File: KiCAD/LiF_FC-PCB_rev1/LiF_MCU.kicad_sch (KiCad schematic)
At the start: 13 parts, among them J4 USB_C_Receptacle_USB2.0_14P, Q3 MMBT4401, Q4 MMBT4401, U4 ESP32-S3-WROOM-1, U5 MCP2200T-E-SS, Y2 12MHz

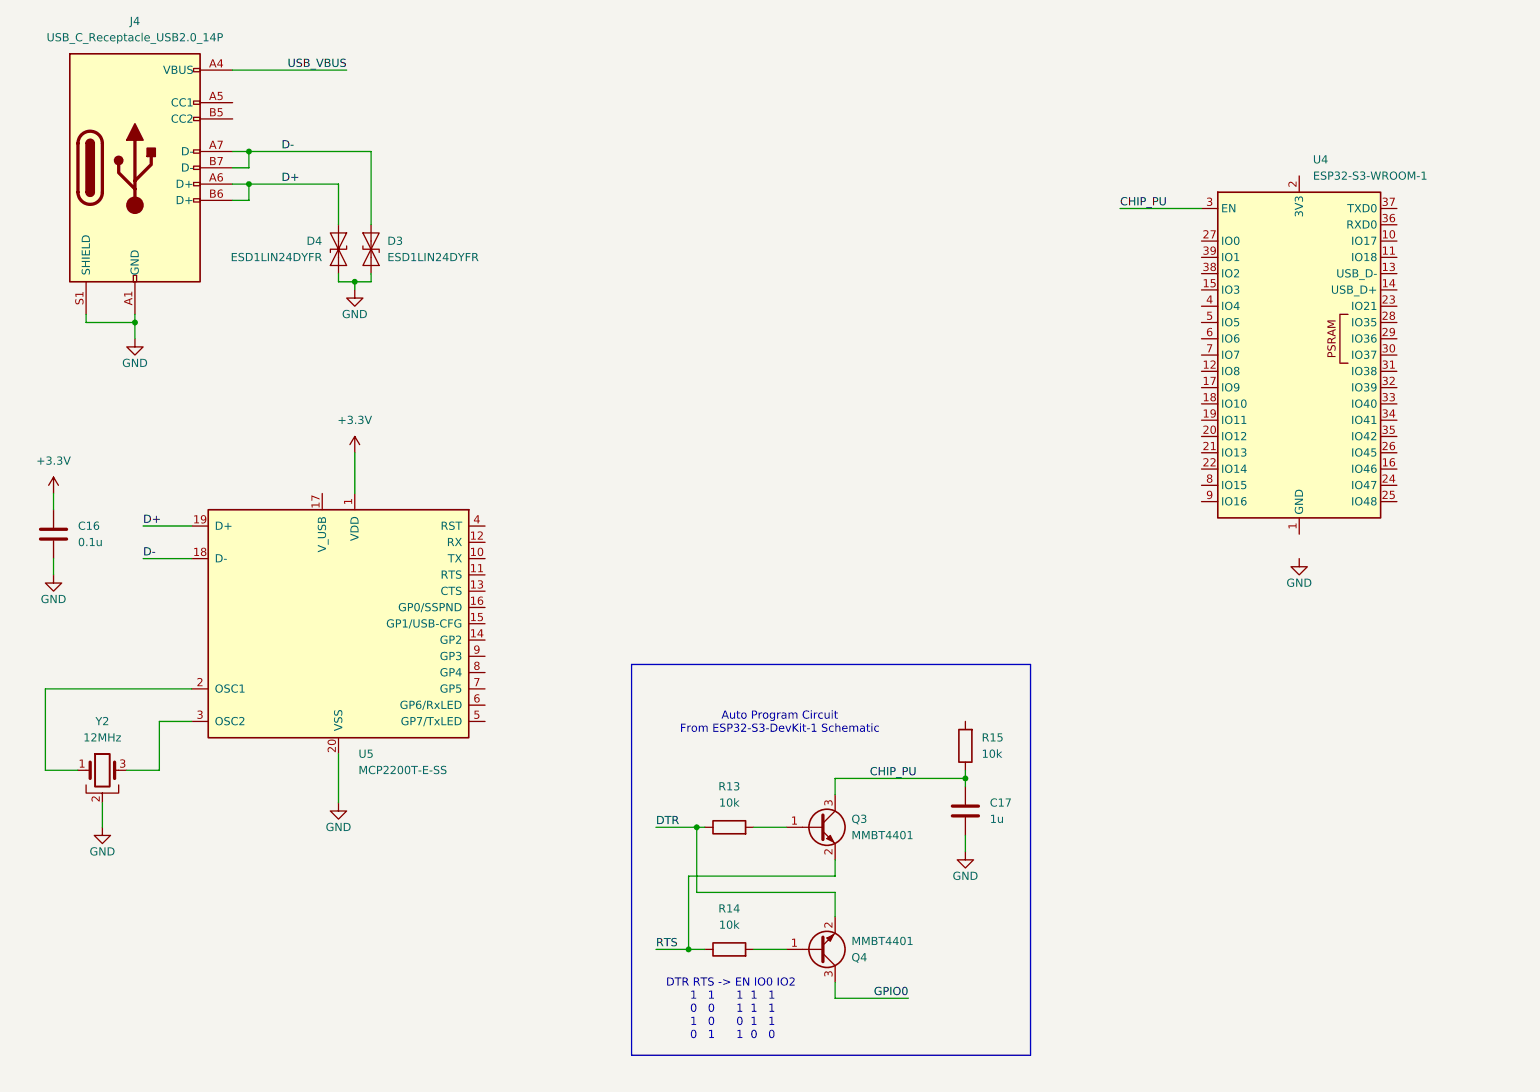
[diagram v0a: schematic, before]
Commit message: replaced a USB to UART bridge to support auto-programming of ESP, added reset and flash buttons
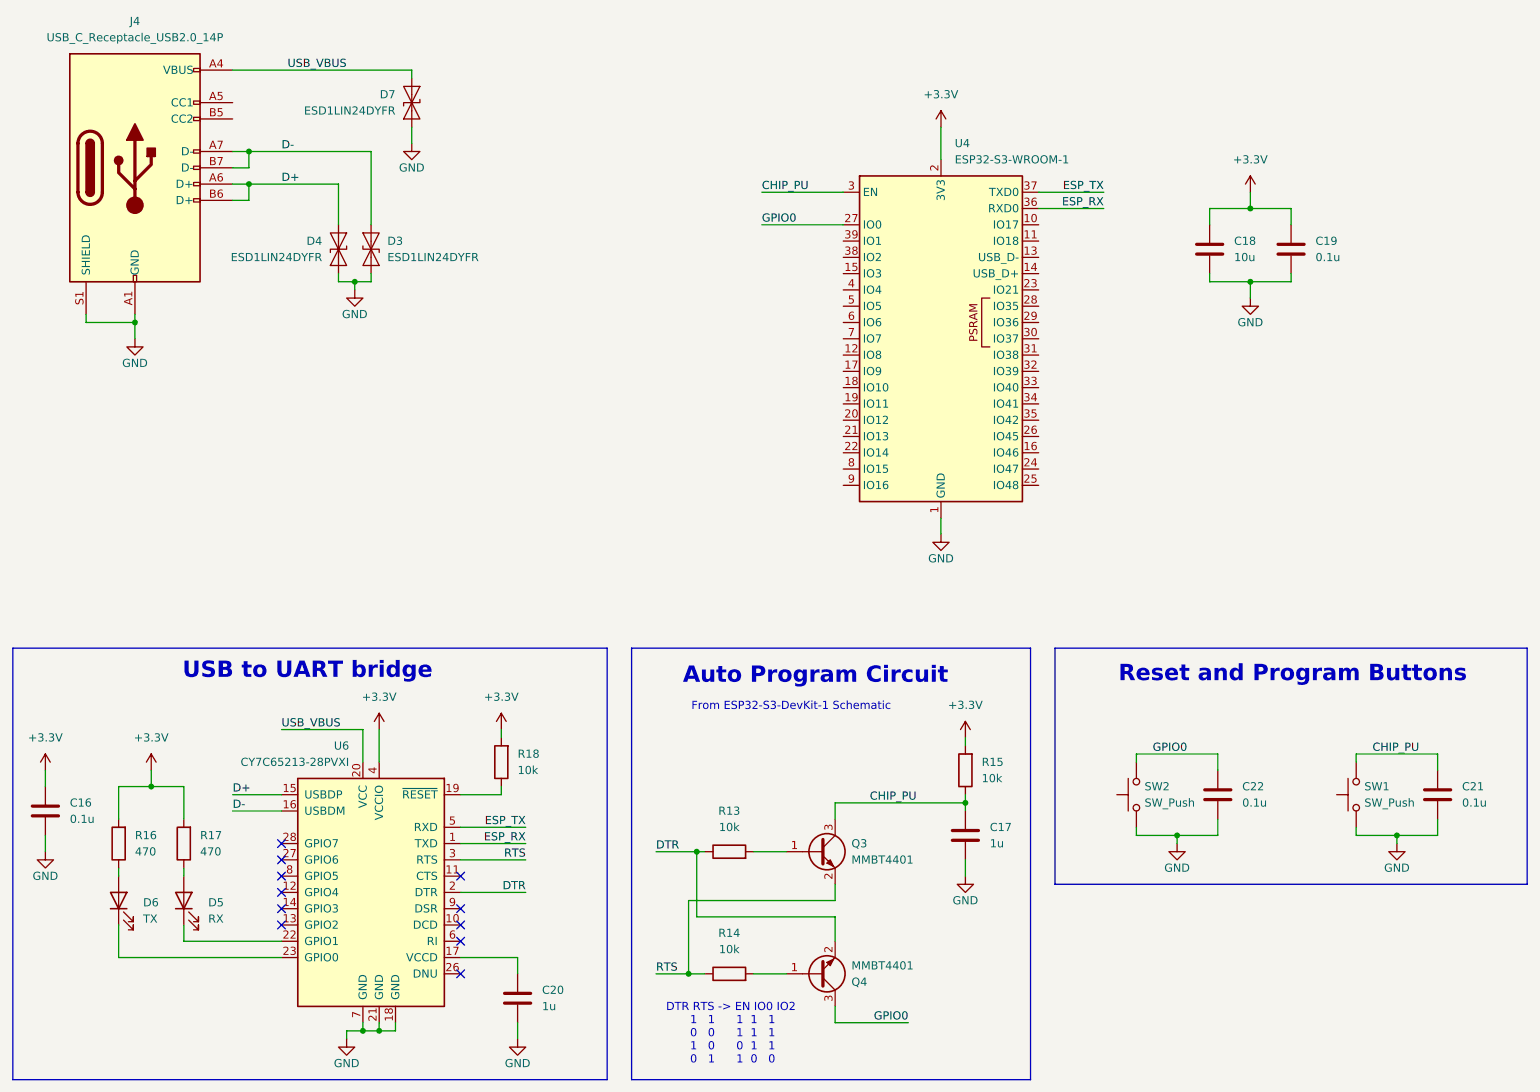
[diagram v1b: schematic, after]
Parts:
- removed U5: MCP2200T-E-SS, Package_SO:SSOP-20_5.3x7.2mm_P0.65mm, symbol Interface_USB:MCP2200T-E-SS
- removed Y2: 12MHz, Crystal:Resonator_SMD_Murata_CSTxExxV-3Pin_3.0x1.1mm, symbol Device:Crystal_GND2
- added C18: 10u, Capacitor_SMD:C_0805_2012Metric, symbol Device:C
- added C19, C21, C22: 0.1u, Capacitor_SMD:C_0805_2012Metric, symbol Device:C
- added C20: 1u, Capacitor_SMD:C_0805_2012Metric, symbol Device:C
- added D5: RX, symbol Device:LED
- added D6: TX, symbol Device:LED
- added D7: ESD1LIN24DYFR, Diode_SMD:D_SOD-323F, symbol Diode:ESD9B5.0ST5G
- added R16, R17: 470, Capacitor_SMD:C_0805_2012Metric, symbol Device:R
- added R18: 10k, Capacitor_SMD:C_0805_2012Metric, symbol Device:R
- added SW1, SW2: SW_Push, symbol Switch:SW_Push
- added U6: CY7C65213-28PVXI, Package_SO:SSOP-28_5.3x10.2mm_P0.65mm, symbol Interface_USB:CY7C65213-28PVXI
- U4: DKPN (none) -> 5407-ESP32-S3-WROOM-1-N16R8CT-ND; PN (none) -> ESP32-S3-WROOM-1-N16R8
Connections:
- net +3.3V: now also R15.2, U4.2 (3V3), C18.1, C19.1, R16.2, R17.2, R18.2, U6.4 (VCCIO)
- net CHIP_PU: now also C21.1, SW1.2
- net D+: now also U6.15 (USBDP)
- net D-: now also U6.16 (USBDM)
- net DTR: now also U6.2 (DTR)
- net GND: now also U4.1 (GND), U4.40 (GND), U4.41 (GND), C18.2, C19.2, C20.2, C21.2, C22.2, D7.1 (A1), SW1.1, SW2.1, U6.18 (GND), U6.21 (GND), U6.7 (GND)
- net GPIO0: now also U4.27 (IO0), C22.1, SW2.2
- net RTS: now also U6.3 (RTS)
- net USB_VBUS: now also D7.2 (A2), U6.20 (VCC)
- net ESP_RX: now reaches U4.36 (RXD0)
- net ESP_RX: now also U6.1 (TXD)
- net ESP_TX: now reaches U4.37 (TXD0)
- net ESP_TX: now also U6.5 (RXD)
- new net: D5.1 (K), U6.22 (GPIO1)
- new net: D5.2 (A), R17.1
- new net: R18.1, U6.19 (~{RESET})
- new net: D6.1 (K), U6.23 (GPIO0)
- new net: D6.2 (A), R16.1
- new net: C20.1, U6.17 (VCCD)
- no-connect marks 0 -> 11
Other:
- note added: "Auto Program Circuit"
- note added: "From ESP32-S3-DevKit-1 Schematic"
- note added: "Reset and Program Buttons"
- note added: "USB to UART bridge"
- note removed: "Auto Program Circuit From ESP32-S3-DevKit-1 Schematic"
- moved on the sheet: C16, C17, Q3, Q4, R13, R14, R15, U4

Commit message: reverted 5V reg, reworked power distribution logic, swapped power OR-ing ICs
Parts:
- added F2: 1A, symbol Device:Polyfuse
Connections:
- net USB_VBUS: now also F2.1
- new net V_{PROG USB}: F2.2
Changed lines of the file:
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@@
+	)
+	(junction
+		(at 77.47 36.83)
+		(diameter 0)
+		(color 0 0 0 0)
 	)
 	(junction
@@
 	(wire
 		(pts
+			(xy 90.17 36.83) (xy 92.71 36.83)
+		)
+		(stroke
+			(width 0)
+			(type default)
+		)
+	)
+	(wire
+		(pts
 			(xy 85.09 165.1) (xy 95.25 165.1)
 		)
@@
 		(pts
 			(xy 26.67 76.2) (xy 34.29 76.2)
+		)
+		(stroke
+			(width 0)
+			(type default)
+		)
+	)
+	(wire
+		(pts
+			(xy 77.47 36.83) (xy 82.55 36.83)
 		)
 		(stroke
@@
 			)
 			(justify right bottom)
+		)
+	)
+	(hierarchical_label "V_{PROG USB}"
+		(shape output)
+		(at 92.71 36.83 0)
+		(effects
+			(font
+				(size 1.27 1.27)
+			)
+			(justify left)
 		)
 	)
@@
 					(unit 1)
 				)
+			)
+		)
+	)
+	(symbol
+		(lib_id "Device:Polyfuse")
+		(at 86.36 36.83 90)
+		(unit 1)
+		(exclude_from_sim no)
+		(in_bom yes)
+		(on_board yes)
+		(dnp no)
+		(fields_autoplaced yes)
+		(property "Reference" "F2"
+			(at 86.36 30.48 90)
+			(effects
+				(font
+					(size 1.27 1.27)
+				)
+			)
+		)
+		(property "Value" "1A"
+			(at 86.36 33.02 90)
+			(effects
+				(font
+					(size 1.27 1.27)
+				)
+			)
+		)
+		(property "Footprint" ""
+			(at 91.44 35.56 0)
+			(effects
+				(font
+					(size 1.27 1.27)
+				)
+				(justify left)
+				(hide yes)
+			)
+		)
+		(property "Datasheet" "~"
+			(at 86.36 36.83 0)
+			(effects
+				(font
+					(size 1.27 1.27)
+				)
+				(hide yes)
+			)
+		)
+		(property "Description" "Resettable fuse, polymeric positive temperature coefficient"
+			(at 86.36 36.83 0)
+			(effects
+				(font
+					(size 1.27 1.27)
+				)
+				(hide yes)
+			)
+		)
+		(pin "2"
+		)
+		(pin "1"
+		)
+		(instances
+			(project "LiF_FC-PCB_rev1"
+				(path "/9e3e8da7-e506-46c9-90e5-307e4ad30d29/fa6eb845-b5e3-4a8e-9c24-c1b567f4e987"
+					(reference "F2")
+					(unit 1)
+				)

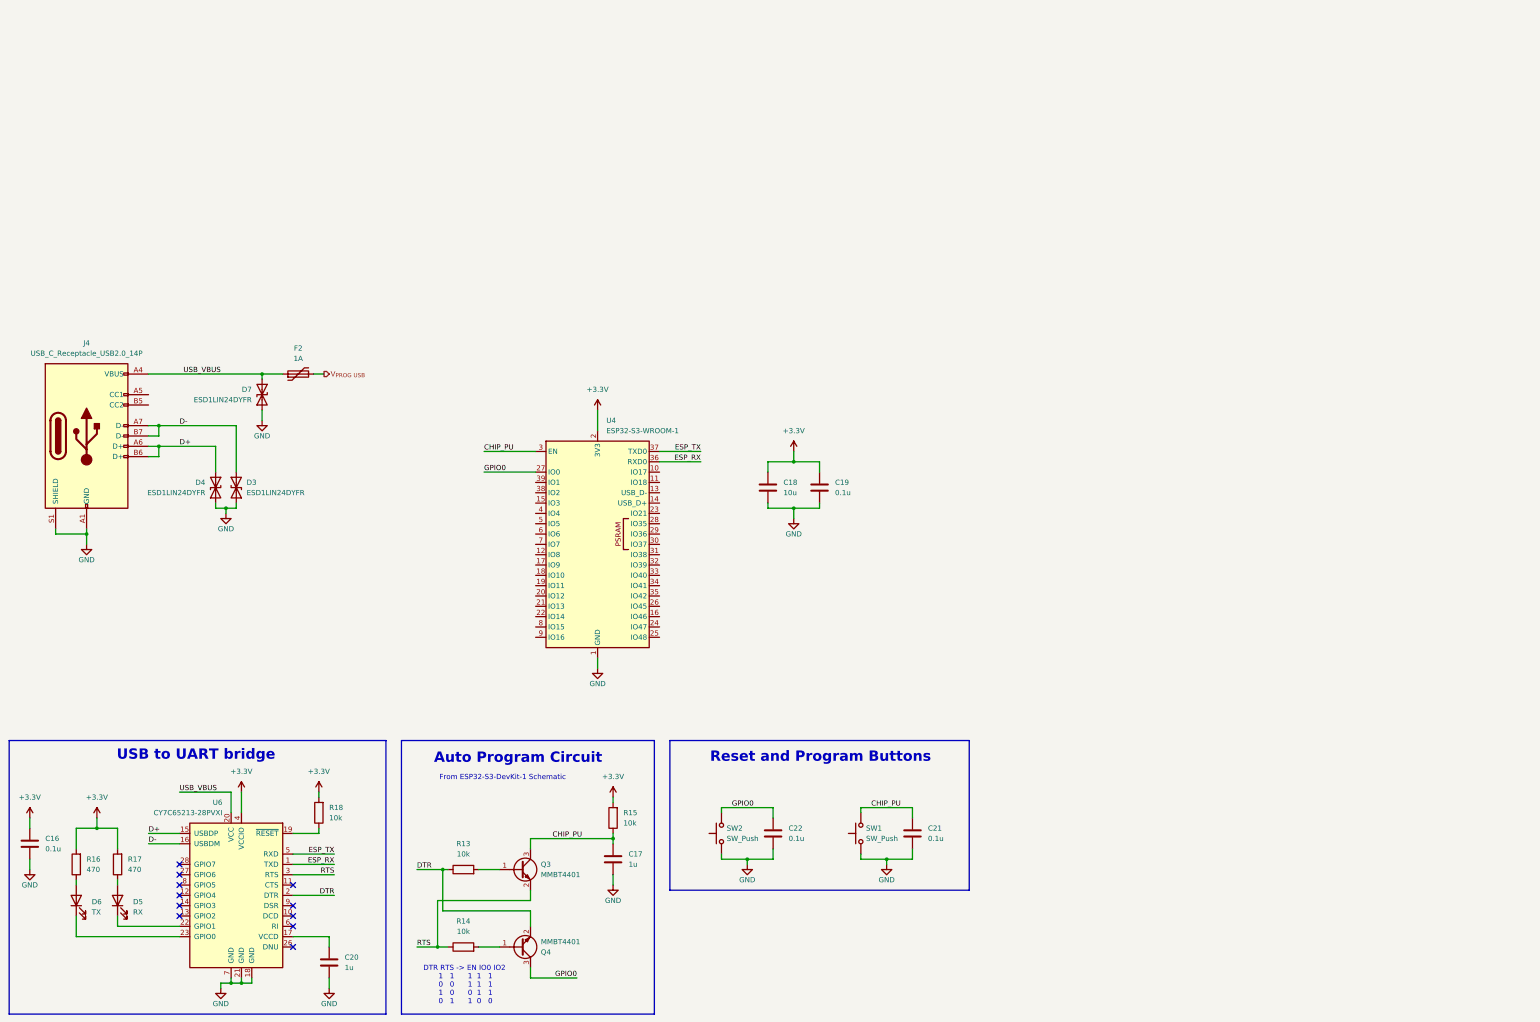
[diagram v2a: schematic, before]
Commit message: Finished schematics, mostly. Only MCU sheet left. Doing component sourcing
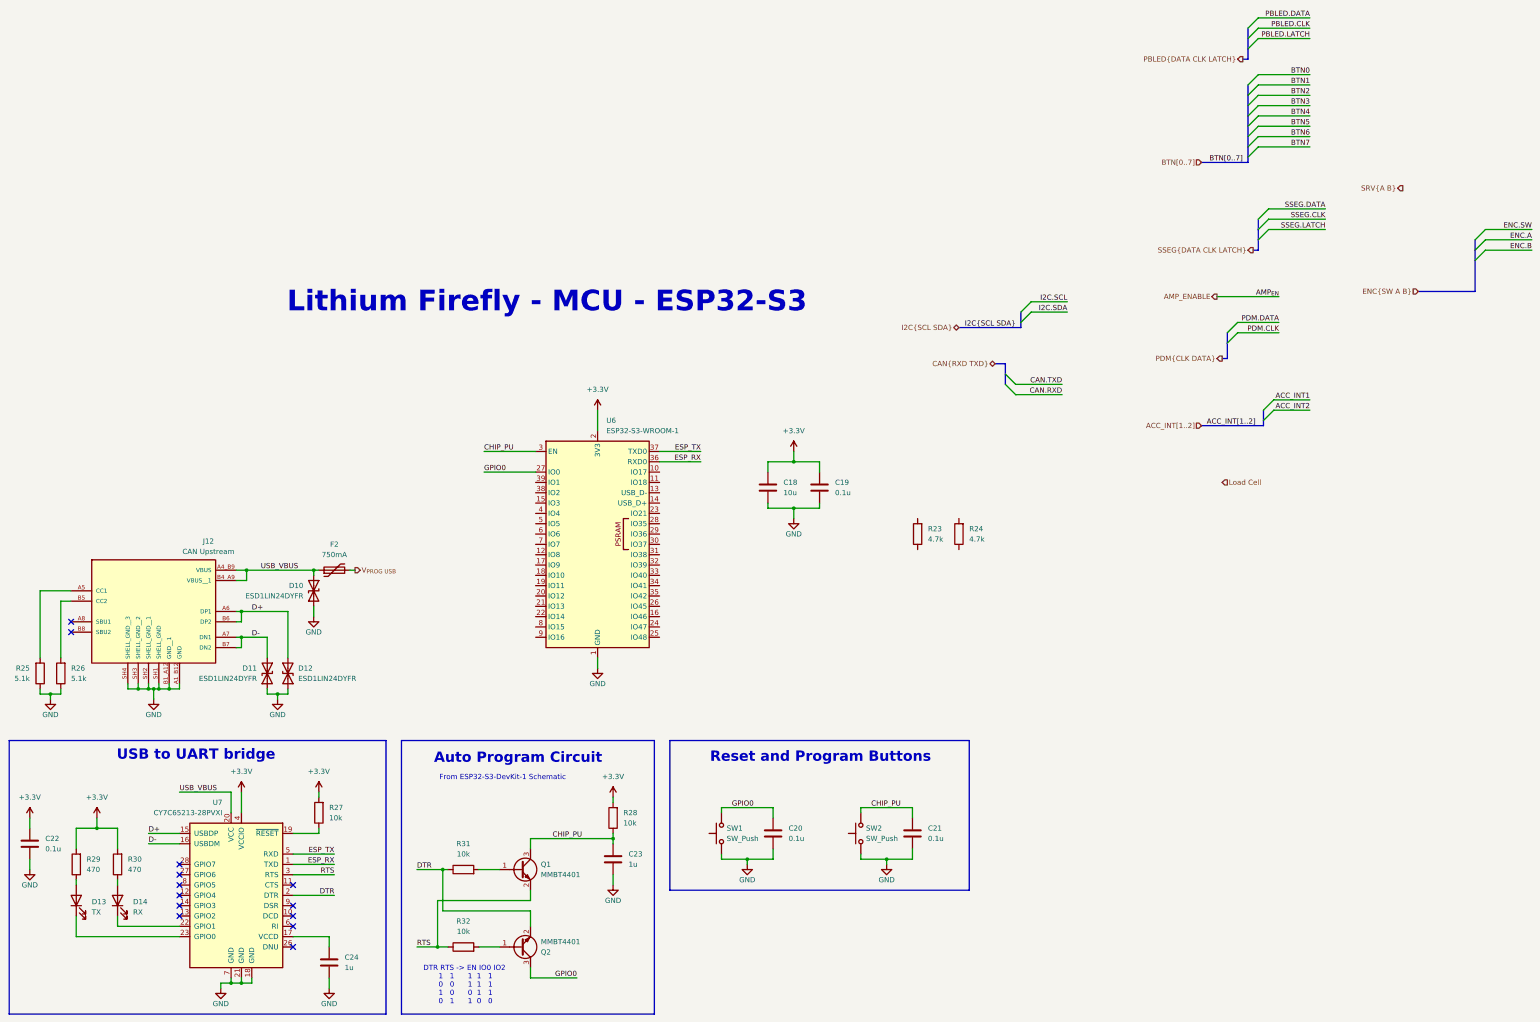
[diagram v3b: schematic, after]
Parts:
- removed J4: USB_C_Receptacle_USB2.0_14P, symbol Connector:USB_C_Receptacle_USB2.0_14P
- added J12: CAN Upstream, LiF_PCB_Footprints:GCT_USB4105-GF-A, symbol LiF_PCB_Symbols:USB4105-GF-A
- added R23, R24: 4.7k, Capacitor_SMD:C_0805_2012Metric, symbol Device:R
- added R25, R26: 5.1k, Capacitor_SMD:C_0805_2012Metric, symbol Device:R
- C18: DKPN (none) -> 490-6473-1-ND; PN (none) -> GRM21BR61C106KE15K
- C19, C21: DKPN (none) -> 490-12005-1-ND; PN (none) -> GRM21BR72A104KAC4L
- C20: renamed from C22; DKPN (none) -> 490-12005-1-ND; PN (none) -> GRM21BR72A104KAC4L
- C22: renamed from C16; DKPN (none) -> 490-12005-1-ND; PN (none) -> GRM21BR72A104KAC4L
- C23: renamed from C17; DKPN (none) -> 490-1691-1-ND; PN (none) -> GRM21BR71C105KA01L
- C24: renamed from C20; DKPN (none) -> 490-1691-1-ND; PN (none) -> GRM21BR71C105KA01L
- D10: renamed from D7; DKPN (none) -> 296-ESD1LIN24DYFRCT-ND; PN (none) -> ESD1LIN24DYFR
- D11: renamed from D4; DKPN (none) -> 296-ESD1LIN24DYFRCT-ND; PN (none) -> ESD1LIN24DYFR
- D12: renamed from D3; DKPN (none) -> 296-ESD1LIN24DYFRCT-ND; PN (none) -> ESD1LIN24DYFR
- D13: renamed from D6; footprint (none) -> LED_SMD:LED_0805_2012Metric; DKPN (none) -> 5366-LC170JRCT-U1CT-ND; PN (none) -> LC170JRCT-U1
- D14: renamed from D5; footprint (none) -> LED_SMD:LED_0805_2012Metric; DKPN (none) -> 5366-LC170JRCT-U1CT-ND; PN (none) -> LC170JRCT-U1
- F2: value 1A -> 750mA; footprint (none) -> Fuse:Fuse_0805_2012Metric; DKPN (none) -> 13-SMD1812B075TF/33CT-ND; PN (none) -> SMD1812B075TF/33
- Q1: renamed from Q3; footprint (none) -> Package_TO_SOT_SMD:SOT-23
- Q2: renamed from Q4; footprint (none) -> Package_TO_SOT_SMD:SOT-23
- SW1: renamed from SW2; footprint (none) -> LiF_PCB_Footprints:SW_TL3301PF160QG; DKPN (none) -> EG4562CT-ND; PN (none) -> TL3301PF160QG
- SW2: renamed from SW1; footprint (none) -> LiF_PCB_Footprints:SW_TL3301PF160QG; DKPN (none) -> EG4562CT-ND; PN (none) -> TL3301PF160QG
- renumbered R18 to R27, R15 to R28, R16 to R29, R17 to R30, R13 to R31, R14 to R32, U4 to U6, U6 to U7
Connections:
- net D+: now also D12.2 (A2), J12.A6 (DP1), J12.B6 (DP2); no longer D11.2 (A2)
- net D-: now also D11.2 (A2), J12.A7 (DN1), J12.B7 (DN2); no longer D12.2 (A2)
- net GND: now also J12.A1_B12 (GND), J12.B1_A12 (GND__1), J12.SH1 (SHELL_GND), J12.SH2 (SHELL_GND__1), J12.SH3 (SHELL_GND__2), J12.SH4 (SHELL_GND__3), R25.1, R26.1
- net USB_VBUS: now also J12.A4_B9 (VBUS), J12.B4_A9 (VBUS__1)
- new net: J12.A5 (CC1), R25.2
- new net: J12.B5 (CC2), R26.2
- no-connect marks 11 -> 13
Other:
- note added: "Lithium Firefly - MCU - ESP32-S3"
- company: (none) -> Lithium Firefly Team
- moved on the sheet: D10, D11, D12, F2

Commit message: fixing ERC bugs on schematic. Only MCU left
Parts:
- added J40: ESP 3V3_{EN}, Connector_PinHeader_2.54mm:PinHeader_1x02_P2.54mm_Vertical, symbol Connector:Conn_01x02_Pin
- added R61: 0, Resistor_SMD:R_0805_2012Metric, symbol Device:R
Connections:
- net +3.3V renamed ESP_3V3
- net ESP_3V3: now also J40.1 (Pin_1), R61.1
- new net 3V3_{IN}: J40.2 (Pin_2), R61.2
- no-connect marks 13 -> 50
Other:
- moved on the sheet: R23, R24
